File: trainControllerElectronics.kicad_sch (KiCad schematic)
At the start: 33 parts, among them IC1 IRF7606TRPBF, J1 ‎WM3436CT-ND‎, J2 USBC, J3 Battery, J4 Debug, J5 Serial, SW1 SW_MEC_5E, SW10 SW_MEC_5E, SW11 SW_MEC_5E, SW12 SW_MEC_5E, SW2 SW_MEC_5E, SW3 SW_MEC_5E, SW4 SW_MEC_5E, SW5 SW_MEC_5E, SW6 SW_MEC_5E, SW7 SW_MEC_5E, SW8 SW_MEC_5E, SW9 SW_MEC_5E, U1 CD74HC4067M96, U3 MCP73831-2-OT

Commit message: library cleaned
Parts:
- R12: value 330R -> 470R
- RV1, RV2, RV3, RV4: footprint Potentiometer_THT:Potentiometer_Bourns_PTV09A-1_Single_Vertical -> ptv09:Potentiometer_Bourns_PTV09A-1_Single_Vertical
- SW1, SW10, SW11, SW12, SW2, SW3, SW4, SW5, SW6, SW7, SW8, SW9: value SW_MEC_5E -> PTS647SM38SMTR2; footprint Button_Switch_SMD:SW_SPST_Omron_B3FS-101xP -> Button_Switch_SMD:SW_SPST_PTS647_Sx38; Digikey part 450-1650-ND -> PTS647SM38SMTR2LFSCT-ND; Manufacturer TE Connectivity ALCOSWITCH Switches -> С&K Components; Manufacturer part 1825910-6 -> PTS647SM38SMTR2 LFS
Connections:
- net KEY_COL_1: now also SW1.1
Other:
- moved on the sheet: A1, J4, J5

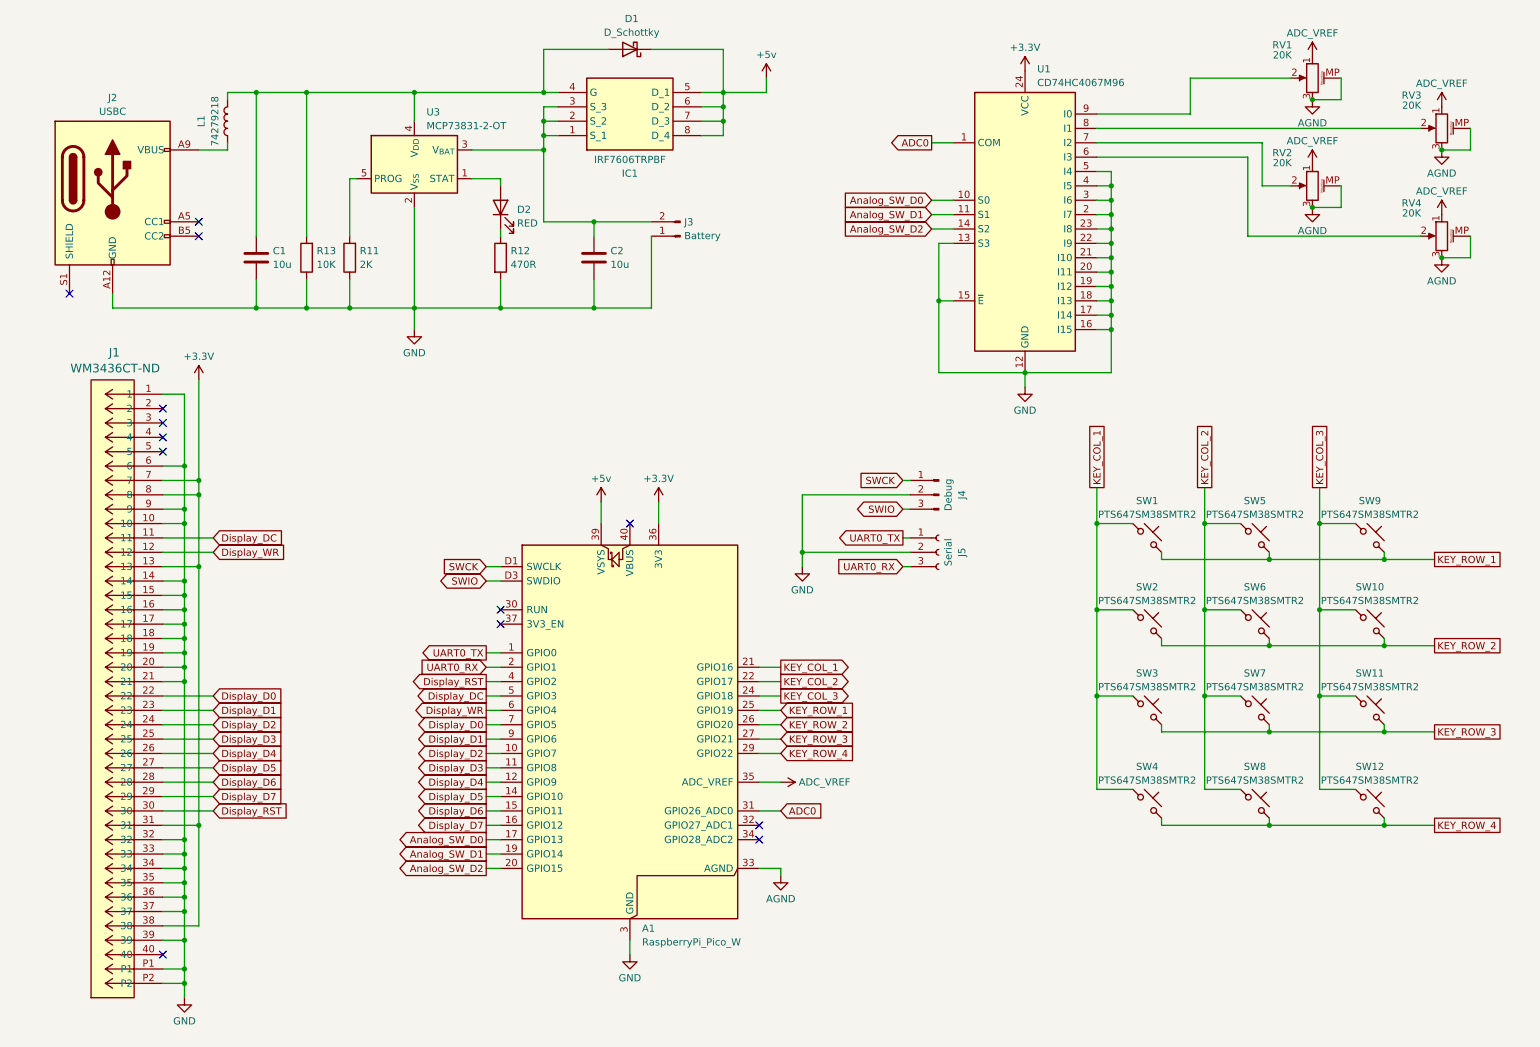
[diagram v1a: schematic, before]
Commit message: New mosfet
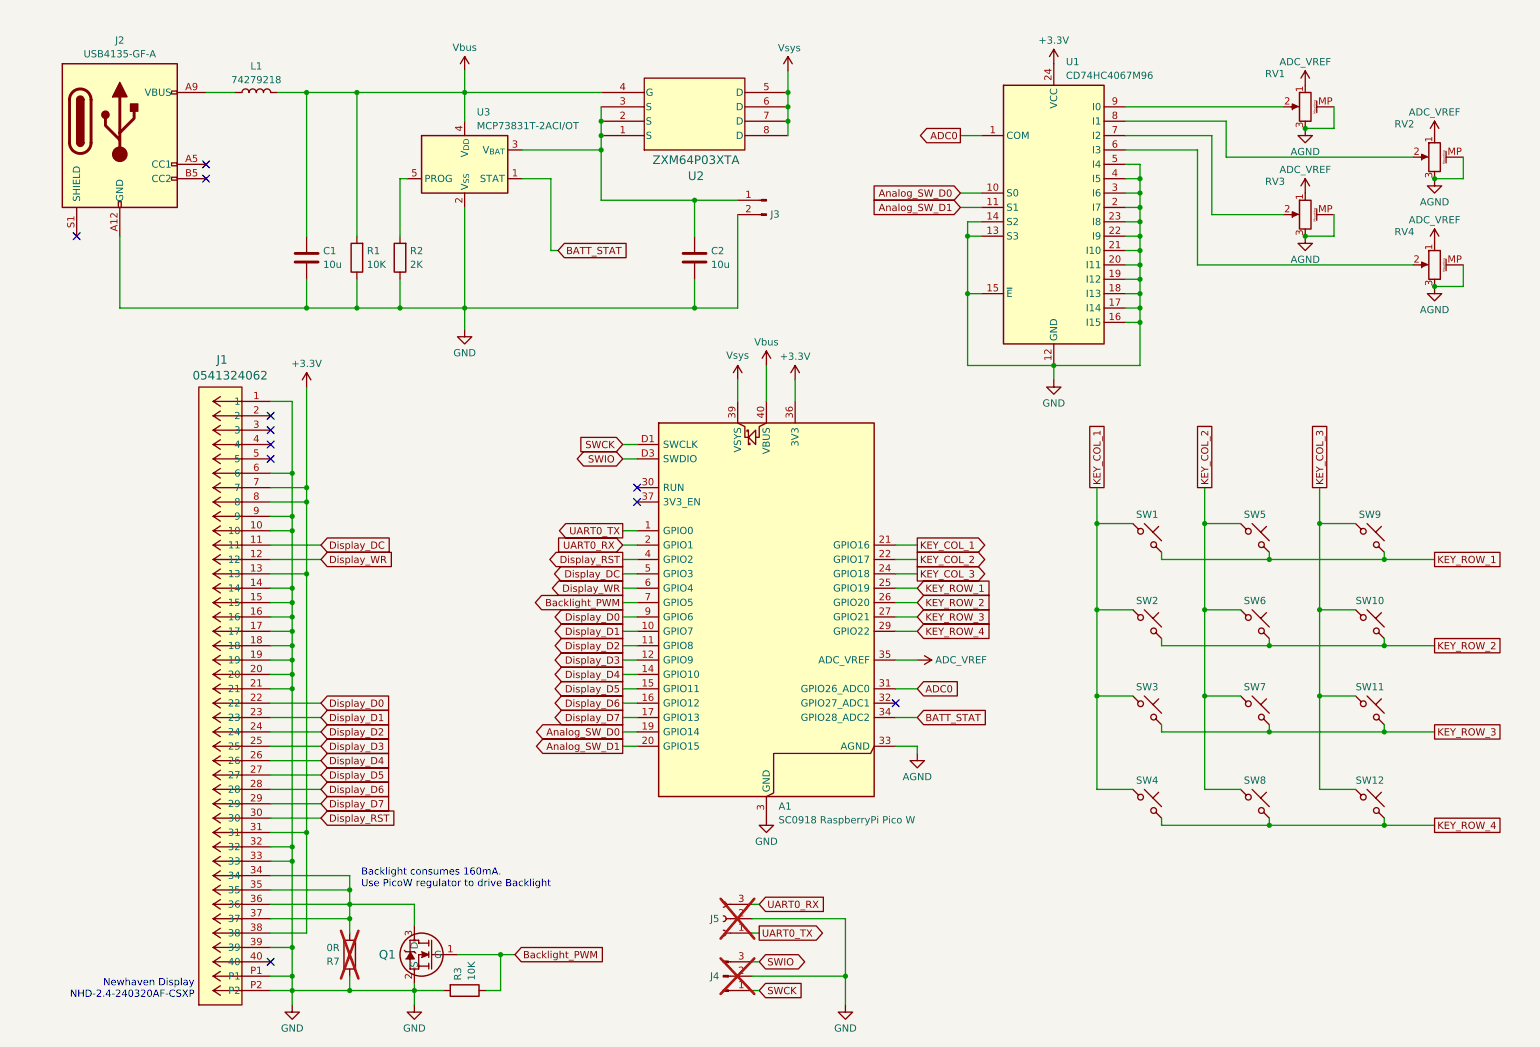
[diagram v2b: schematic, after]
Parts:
- removed D1: D_Schottky, PMEG4010AESBYL:DIODFN100X60X30-2N, symbol Device:D_Schottky
- removed D2: RED, LED_SMD:LED_0805_2012Metric_Pad1.15x1.40mm_HandSolder, symbol Device:LED
- removed IC1: IRF7606TRPBF, IRF7606TRPBF:SOP65P490X111-8N, symbol IRF7606TRPBF:IRF7606TRPBF
- removed R12: 470R, Resistor_SMD:R_0805_2012Metric_Pad1.20x1.40mm_HandSolder, symbol Device:R
- added Q1: BSS670S2LH6327XTSA1, BSS670S2L:PG-SOT23-3-5_INF, symbol BSS670S2L:BSS670S2LH6327XTSA1
- added R3: 10K, Resistor_SMD:R_0805_2012Metric_Pad1.20x1.40mm_HandSolder, symbol Device:R
- added R7: 0R, Resistor_SMD:R_0805_2012Metric_Pad1.20x1.40mm_HandSolder, symbol Device:R
- added U2: ZXM64P03XTA, SOIC8_ZXM64P03X_DIO, symbol ZXM64P03XTA:ZXM64P03XTA
- A1: value RaspberryPi_Pico_W -> SC0918 RaspberryPi Pico W; Digikey part (none) -> 2648-SC0918CT-ND; Manufacturer (none) -> Raspberry Pi; Manufacturer part (none) -> SC0918
- J1: value ‎WM3436CT-ND‎ -> 0541324062; Digikey part (none) -> ‎WM3436CT-ND‎; Manufacturer (none) -> Molex; Manufacturer part (none) -> 0541324062
- J2: value USBC -> USB4135-GF-A; Digikey part (none) -> 2073-USB4135-GF-ACT-ND; Manufacturer (none) -> CGT; Manufacturer part (none) -> USB4135-GF-A
- J3: value Battery -> B2B-PH-K-S; footprint Connector_JST:JST_XH_B2B-XH-A_1x02_P2.50mm_Vertical -> Connector_JST:JST_PH_B2B-PH-K_1x02_P2.00mm_Vertical; Digikey part (none) -> 455-1704-ND; Manufacturer (none) -> JST; manufacturer part (none) -> B2B-PH-K-S
- J4: value Debug -> Pin header 2.54 1x03; now not fitted
- J5: value Serial -> Pin socket 2.54 1x03; now not fitted
- RV1, RV2, RV3, RV4: value 20K -> PTV09A-4015F-B104‎; Digikey part 118-PTV09A-4015F-B203-ND -> PTV09A-4015F-B104-ND‎; Manufacturer part PTV09A-4015F-B203 -> PTV09A-4015F-B104‎
- SW1, SW10, SW11, SW12, SW2, SW3, SW4, SW5, SW6, SW7, SW8, SW9: value PTS647SM38SMTR2 -> PTS647SM38SMTR2 LFS
- U1: Digikey part (none) -> 296-29408-1-ND; Manufacturer (none) -> Texas Instruments; Manufacturer part (none) -> CD74HC4067M96
- U3: value MCP73831-2-OT -> MCP73831T-2ACI/OT; Digikey part (none) -> MCP73831T-2ACI/OTCT-ND; Manufacturer (none) -> Microchip; Manufacturer part (none) -> MCP73831T-2ACI/OT
- renumbered R13 to R1, R11 to R2
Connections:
- net Analog_SW_D0: now also A1.19 (GPIO14); no longer A1.17 (GPIO13)
- net Analog_SW_D1: now also A1.20 (GPIO15); no longer A1.19 (GPIO14)
- net Display_D0: now also A1.9 (GPIO6); no longer A1.7 (GPIO5)
- net Display_D1: now also A1.10 (GPIO7); no longer A1.9 (GPIO6)
- net Display_D2: now also A1.11 (GPIO8); no longer A1.10 (GPIO7)
- net Display_D3: now also A1.12 (GPIO9); no longer A1.11 (GPIO8)
- net Display_D4: now also A1.14 (GPIO10); no longer A1.12 (GPIO9)
- net Display_D5: now also A1.15 (GPIO11); no longer A1.14 (GPIO10)
- net Display_D6: now also A1.16 (GPIO12); no longer A1.15 (GPIO11)
- net Display_D7: now also A1.17 (GPIO13); no longer A1.16 (GPIO12)
- net GND: now also J3.2 (Pin_2), U1.14 (S2), Q1.2 (S), R3.2, R7.2; no longer J1.34, J1.35, J1.36, J1.37, J3.1 (Pin_1)
- net Vbus: now reaches C1.1, L1.2, R1.2, U3.4 (V_{DD})
- net Vbus: now also A1.40 (VBUS), U2.4 (G)
- net at U1.7 (I2): now also RV3.2; no longer RV2.2
- net at U1.8 (I1): now also RV2.2; no longer RV3.2
- net at C2.1, U3.3 (V_{BAT}): now also J3.1 (Pin_1), U2.1 (S), U2.2 (S), U2.3 (S); no longer J3.2 (Pin_2)
- net BATT_STAT: now reaches U3.1 (STAT)
- net BATT_STAT: now also A1.34 (GPIO28_ADC2)
- net +5v renamed Vsys
- net Vsys: now also U2.5 (D), U2.6 (D), U2.7 (D), U2.8 (D)
- removed net Analog_SW_D2: A1.20 (GPIO15), U1.14 (S2)
- new net: J1.34, J1.35, J1.36, J1.37, Q1.3 (D), R7.1
- new net Backlight_PWM: A1.7 (GPIO5), Q1.1 (G), R3.1
- no-connect marks 13 -> 11
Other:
- note added: "Backlight consumes 160mA. Use PicoW regulator to drive Backlight"
- note added: "Newhaven Display NHD-2.4-240320AF-CSXP"
- moved on the sheet: A1, C1, C2, J1, J2, J3, L1, R1, R2, RV1, U1, U3

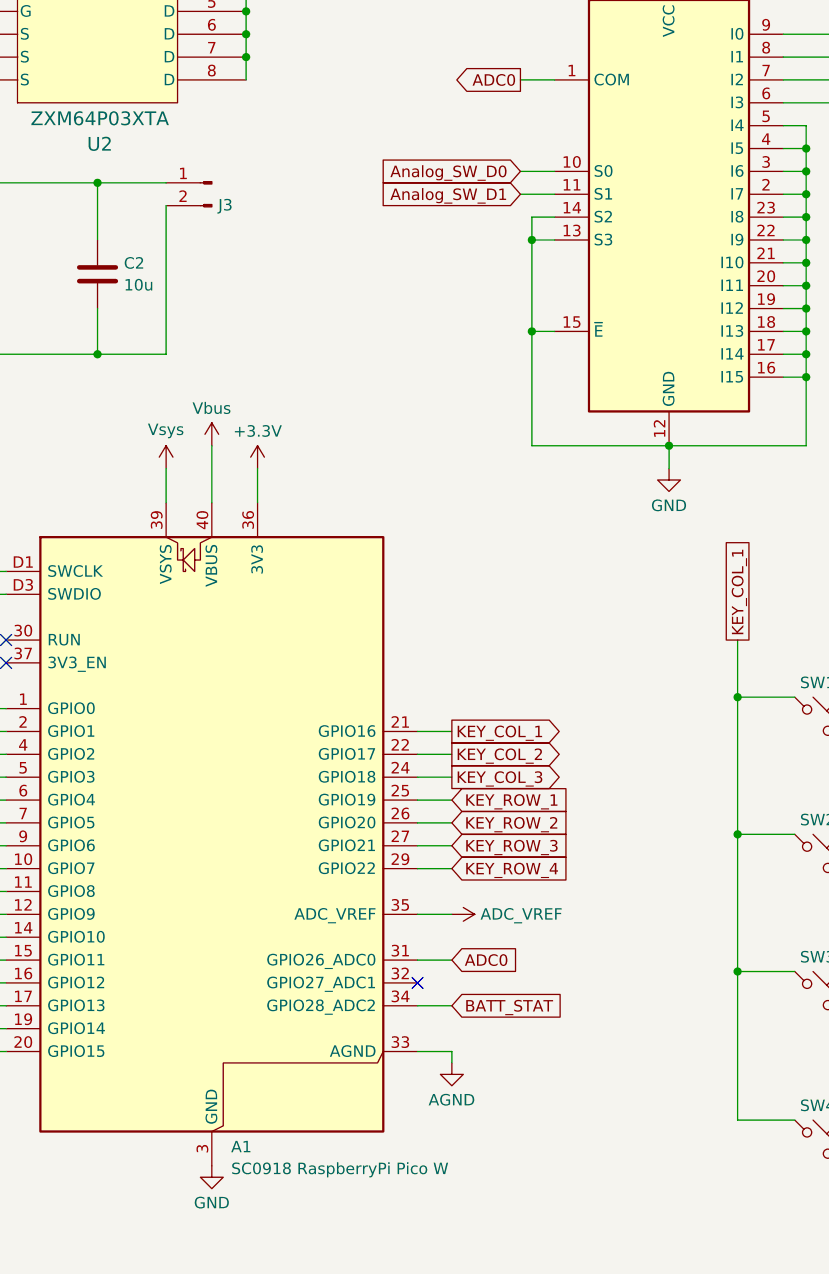
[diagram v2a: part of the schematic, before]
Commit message: Added Battery meter
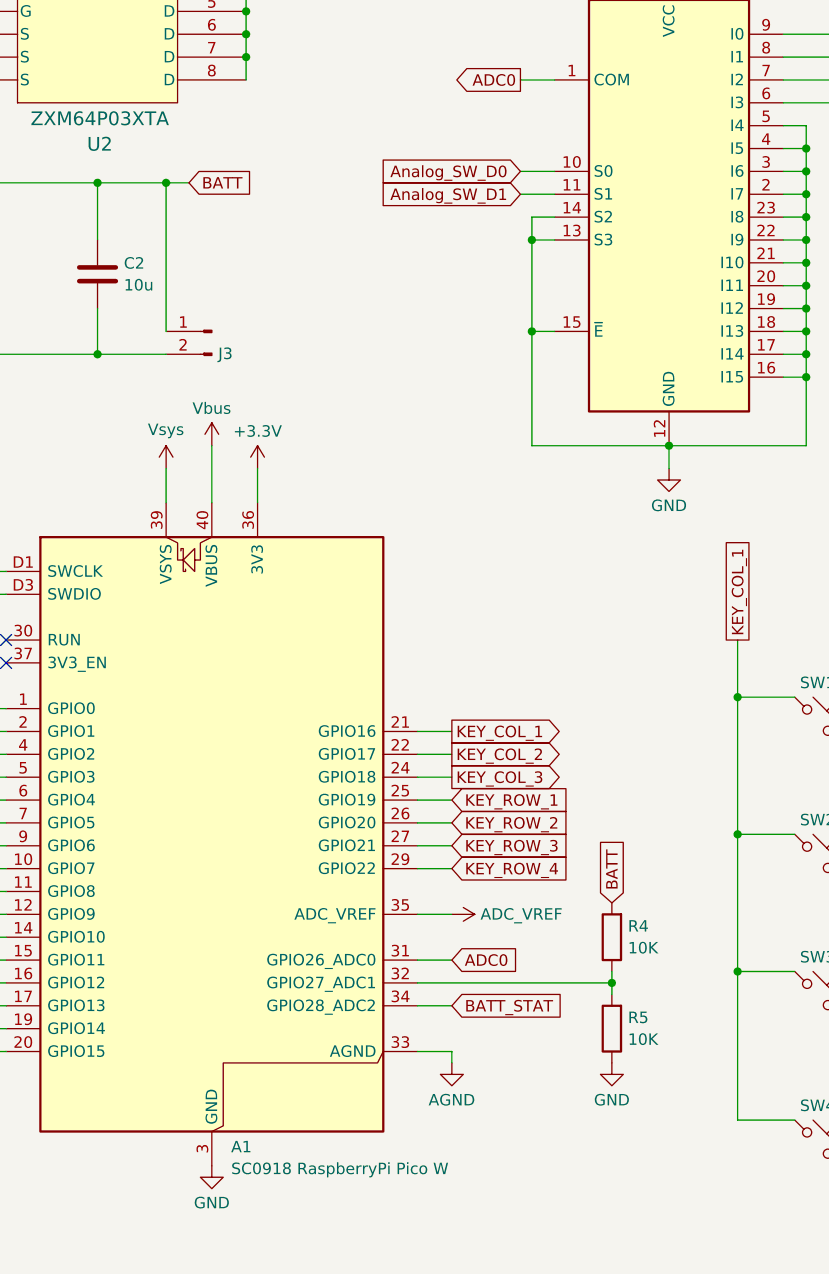
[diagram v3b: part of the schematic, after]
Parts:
- added R4, R5: 10K, Resistor_SMD:R_0805_2012Metric_Pad1.20x1.40mm_HandSolder, symbol Device:R
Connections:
- net GND: now also R5.1
- net BATT: now reaches C2.1, J3.1 (Pin_1), U2.1 (S), U2.2 (S), U2.3 (S), U3.3 (V_{BAT})
- net BATT: now also R4.2
- net at A1.32 (GPIO27_ADC1): now also R4.1, R5.2
- no-connect marks 11 -> 10
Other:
- moved on the sheet: J3

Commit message: PCB ready
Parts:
- removed C1, C2: 10u, Capacitor_SMD:C_0805_2012Metric_Pad1.18x1.45mm_HandSolder, symbol Device:C
- removed J2: USB4135-GF-A, Connector_USB:USB_C_Receptacle_GCT_USB4135-GF-A_6P_TopMnt_Horizontal, symbol Connector:USB_C_Receptacle_PowerOnly_6P
- removed J3: B2B-PH-K-S, Connector_JST:JST_PH_B2B-PH-K_1x02_P2.00mm_Vertical, symbol Connector:Conn_01x02_Pin
- removed L1: 74279218, Inductor_SMD:L_1206_3216Metric_Pad1.42x1.75mm_HandSolder, symbol Device:L
- removed Q1: BSS670S2LH6327XTSA1, BSS670S2L:PG-SOT23-3-5_INF, symbol BSS670S2L:BSS670S2LH6327XTSA1
- removed R1, R3: 10K, Resistor_SMD:R_0805_2012Metric_Pad1.20x1.40mm_HandSolder, symbol Device:R
- removed SW10, SW11, SW12, SW7, SW8, SW9: PTS647SM38SMTR2 LFS, Button_Switch_SMD:SW_SPST_PTS647_Sx38, symbol Switch:SW_Push_45deg
- removed U2: ZXM64P03XTA, SOIC8_ZXM64P03X_DIO, symbol ZXM64P03XTA:ZXM64P03XTA
- removed U3: MCP73831T-2ACI/OT, Package_TO_SOT_SMD:SOT-23-5, symbol Battery_Management:MCP73831-2-OT
- added R4: 10K, Resistor_SMD:R_0805_2012Metric_Pad1.20x1.40mm_HandSolder, symbol Device:R
- added R5: 0R, Resistor_SMD:R_0805_2012Metric_Pad1.20x1.40mm_HandSolder, symbol Device:R
- R2: value 2K -> 10K
- SW1, SW2, SW3, SW4, SW5, SW6: value PTS647SM38SMTR2 LFS -> 1825910-6; footprint Button_Switch_SMD:SW_SPST_PTS647_Sx38 -> Button_Switch_THT:SW_PUSH_6mm; Digikey part PTS647SM38SMTR2LFSCT-ND -> 450-1650-ND; Manufacturer С&K Components -> TE CONNECTIVITY; Manufacturer part PTS647SM38SMTR2 LFS -> 1825910-6
- renumbered J5 to J1, J4 to J2, J1 to J3, R4 to R1, R5 to R3, R7 to R6, A1 to U2
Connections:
- net AGND: now also U1.16 (I15), U1.17 (I14), U1.18 (I13), U1.19 (I12), U1.2 (I7), U1.20 (I11), U1.21 (I10), U1.22 (I9), U1.23 (I8), U1.3 (I6), U1.4 (I5), U1.5 (I4)
- net Analog_SW_D0: now also U2.27 (GPIO21); no longer U2.19 (GPIO14)
- net Analog_SW_D1: now also U2.29 (GPIO22); no longer U2.20 (GPIO15)
- net BATT_STAT: now also R2.2; no longer U2.34 (GPIO28_ADC2)
- net Display_RST: now also U2.6 (GPIO4); no longer U2.4 (GPIO2)
- net Display_WR: now also U2.4 (GPIO2); no longer U2.6 (GPIO4)
- net GND: now also R4.1; no longer R2.1, U1.16 (I15), U1.17 (I14), U1.18 (I13), U1.19 (I12), U1.2 (I7), U1.20 (I11), U1.21 (I10), U1.22 (I9), U1.23 (I8), U1.3 (I6), U1.4 (I5), U1.5 (I4)
- net KEY_COL_1: now also U2.19 (GPIO14); no longer SW2.1, SW3.1, U2.21 (GPIO16)
- net KEY_COL_2: now also SW2.1, U2.20 (GPIO15); no longer SW6.1, U2.22 (GPIO17)
- net KEY_COL_3: now also SW3.1, SW6.1, U2.21 (GPIO16); no longer U2.24 (GPIO18)
- net KEY_ROW_1: now also SW2.2, SW3.2, U2.22 (GPIO17); no longer SW5.2, U2.25 (GPIO19)
- net KEY_ROW_2: now also SW4.2, SW5.2, U2.24 (GPIO18); no longer SW2.2, U2.26 (GPIO20)
- net at J3.34, J3.35, J3.36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: now also R5.1
- net at R1.1, R3.2: now also U2.31 (GPIO26_ADC0); no longer U2.32 (GPIO27_ADC1)
- net ADC0 renamed ADC2
- net ADC2: now also U2.34 (GPIO28_ADC2); no longer U2.31 (GPIO26_ADC0)
- net BATT renamed Vbat
- removed net KEY_ROW_3: SW3.2, U2.27 (GPIO21)
- removed net KEY_ROW_4: SW4.2, U2.29 (GPIO22)
- net Vsys: no longer names the net of U2.39 (VSYS)
- new net: R2.1, R4.2, U2.32 (GPIO27_ADC1)
- new net Backlight_Cathode: R5.2
- new net Soft_Power: U2.25 (GPIO19)
- no-connect marks 10 -> 9
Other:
- added sheet Power Supply (Power.Supply_sch.kicad_sch)
- note added: "Backlight consumes 160mA. We use PicoW regulator to drive Backlight."
- note removed: "Backlight consumes 160mA. Use PicoW regulator to drive Backlight"
- moved on the sheet: J1, J2, J3, R1, R3, R6, RV2, RV4, U1, U2
